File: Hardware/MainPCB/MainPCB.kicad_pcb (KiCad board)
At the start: 2 copper layers, 44 parts, among them J1 USB_B_Micro, J2 Conn_01x09_Female, J3 UART, Q1 NTR2101P, Q2 FDS9926A, U1 BQ24075, U2 BQ29700, U3 TLV75533PDBV, U4 ESP32-WROOM-32D, U5 TPS22919

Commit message: Eerste plaatsing van componenten op PCB
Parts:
- added C12: 10u/16V, Capacitor_SMD:CP_Elec_4x5.4, F.Cu at (55.8, 123.1)
- added C16: 3.3u/16V, Capacitor_SMD:CP_Elec_4x5.4, F.Cu at (55.8, 128.9)
- added C17: 3.3u/16V, Capacitor_SMD:CP_Elec_4x5.4, F.Cu at (63.6, 123.1)
- added C18: 10u/16V, Capacitor_SMD:CP_Elec_4x5.4, F.Cu at (63.6, 128.9)
- added C19: 10u/16V, Capacitor_SMD:CP_Elec_4x5.4, F.Cu at (71.3, 123.1)
- added R13: 680, Resistor_SMD:R_1206_3216Metric_Pad1.42x1.75mm_HandSolder, F.Cu at (54.9, 133.5)
- added R14: 680, Resistor_SMD:R_1206_3216Metric_Pad1.42x1.75mm_HandSolder, F.Cu at (60.9, 133.5)
- added U6: TPS22919, Package_TO_SOT_SMD:SOT-363_SC-70-6, F.Cu at (73.1, 113.9)
- added U7: TPS22919, Package_TO_SOT_SMD:SOT-363_SC-70-6, F.Cu at (80.9, 108.1)
- C10: value 47u -> 47u/10V
- C11, C13: value 100nF -> 0.1u
- C14: value 1u -> 3.3u/16V; footprint Capacitor_SMD:C_1206_3216Metric_Pad1.42x1.75mm_HandSolder -> Capacitor_SMD:CP_Elec_4x5.4
- C15: value 10u -> 10u/16V; footprint Capacitor_SMD:C_1206_3216Metric_Pad1.42x1.75mm_HandSolder -> Capacitor_SMD:CP_Elec_4x5.4
- C2: value 47u -> 47u/16V; footprint Capacitor_SMD:CP_Elec_5x5.9 -> Capacitor_SMD:CP_Elec_5x5.4
- C7: value 47u -> 47u/16V; footprint Capacitor_SMD:CP_Elec_4x5.4 -> Capacitor_SMD:CP_Elec_5x5.4
- JP1: value Jumper -> Stroommeetdraad
- moved C15 82.0 mm to (77.4, 129.3), turned to 180 degrees
- moved R11 81.4 mm to (81.1, 136.6), turned to 180 degrees
- moved U5 80.6 mm to (79.8, 115.0), turned to 180 degrees
- moved R12 79.7 mm to (81.1, 133.3), turned to 180 degrees
- moved J3 70.9 mm to (86.4, 135.9), turned to 180 degrees
- moved C11 70.2 mm to (84.9, 126.7), turned to 180 degrees
- moved U3 66.9 mm to (104.4, 99.4), turned to 270 degrees
- moved C2 65.7 mm to (136.7, 86.7), turned to 90 degrees
- moved D1 64.5 mm to (147.0, 103.4), turned to 90 degrees
- moved D2 60.3 mm to (147.0, 97.3), turned to 90 degrees
- moved C13 58.4 mm to (90.8, 126.9), turned to 180 degrees
- moved C12 58.2 mm to (90.8, 123.6), turned to 180 degrees
- moved EN1 55.1 mm to (94.2, 134.4), turned to 180 degrees
- moved R1 55.1 mm to (135.1, 95.7), turned to 90 degrees
- moved R2 52.4 mm to (126.7, 91.8), turned to 90 degrees
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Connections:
- C13 pad 1: +3V3 -> GND
- C13 pad 2: GND -> +3V3
- U4 pad 23: Net-(U4-Pad23) -> PowerS1
- U4 pad 27: Net-(U4-Pad27) -> PowerS2
- U4 pad 28: Net-(U4-Pad28) -> PowerS3
- U5 pad 3: Net-(U5-Pad3) -> PowerS1
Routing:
- net VSS: track 0.00 -> 66.7 mm
- net Net-(BT1-Pad2): track 0.00 -> 33.8 mm
- net +BATT: track 0.00 -> 30.7 mm
- net VDD1: track 0.00 -> 19.6 mm
- net Net-(Q2-Pad4): track 0.00 -> 19.2 mm
- net Vin: track 0.00 -> 18.4 mm
- net VDD2: track 0.00 -> 7.54 mm
- net Net-(Q2-Pad2): track 0.00 -> 6.79 mm
- net Net-(C8-Pad1): track 0.00 -> 6.63 mm
- net GND: track 0.00 -> 6.46 mm
- net Net-(Q2-Pad5): track 0.00 -> 3.81 mm
- net +3V3: track 0.00 -> 2.90 mm
- net Net-(R8-Pad1): track 0.00 -> 2.67 mm
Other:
- board outline added: 99.1 x 103.9 mm
- rule trace_min: 0.2 -> 0

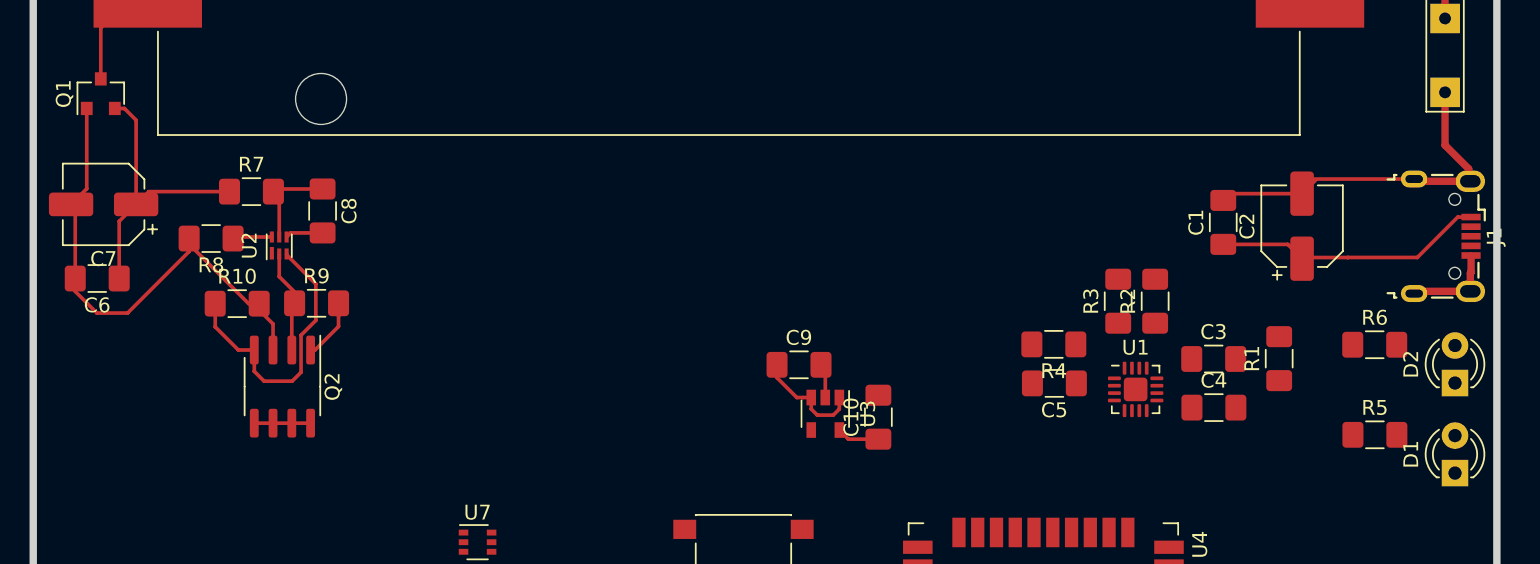
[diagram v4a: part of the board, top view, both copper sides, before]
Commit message: Aux pin verwijderd + aanpassing gedaan VSS naar -VBAT en GND op de juiste plaats gezet
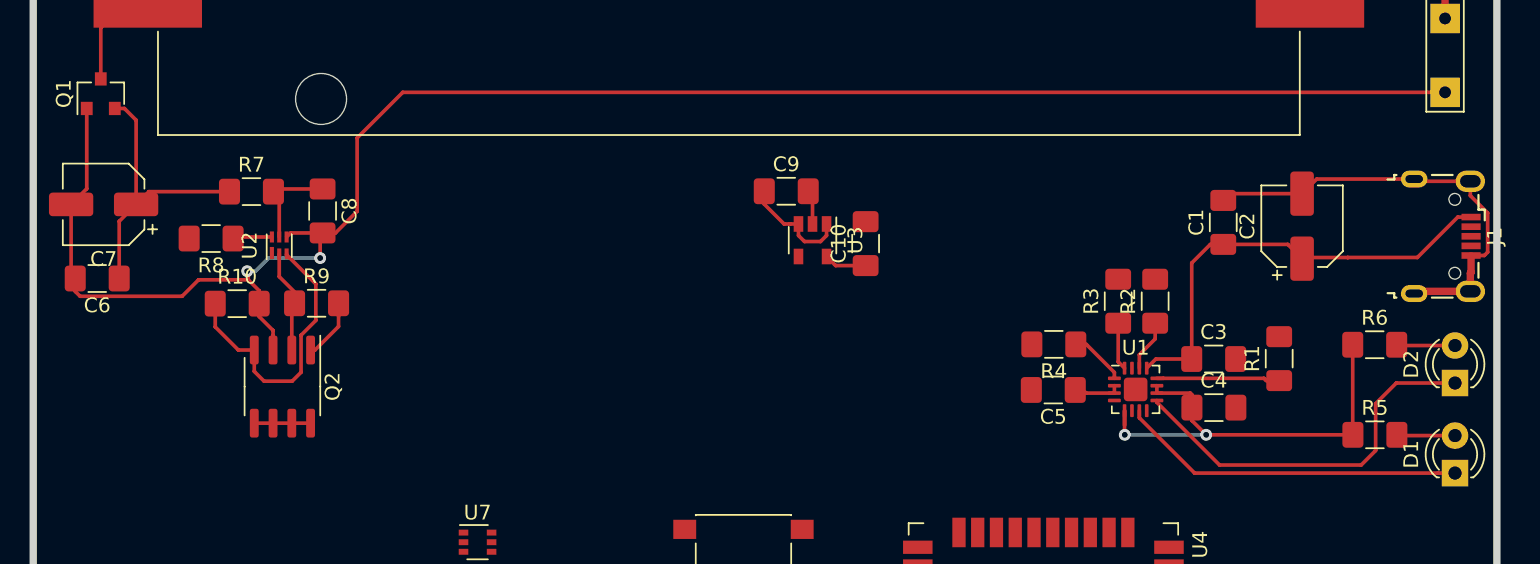
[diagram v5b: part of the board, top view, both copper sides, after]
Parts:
- moved C9 11.8 mm to (101.8, 84.3)
- moved U3 11.8 mm to (103.5, 87.6)
- moved C10 11.8 mm to (107.1, 87.9)
- moved C5 0.45 mm to (119.8, 97.8)
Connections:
- C1 pad 2: VSS -> GND
- C2 pad 2: VSS -> GND
- C3 pad 2: VSS -> Net-(C3-Pad2)
- C4 pad 2: VSS -> GND
- C5 pad 2: VSS -> GND
- C6 pad 2: VSS -> -BATT
- C7 pad 2: VSS -> -BATT
- C8 pad 2: VSS -> -BATT
- J1 pad 5: VSS -> GND
- J1 pad 6: VSS -> GND
- JP1 pad 2: VSS -> -BATT
- Q1 pad 1: VSS -> -BATT
- Q2 pad 3: VSS -> -BATT
- R1 pad 2: VSS -> GND
- R10 pad 2: VSS -> -BATT
- R2 pad 2: VSS -> GND
- R3 pad 2: VSS -> GND
- R4 pad 2: VSS -> GND
- R8 pad 2: VSS -> GND
- U1 pad 15: VSS -> GND
- U1 pad 17: VSS -> GND
- U1 pad 4: VSS -> GND
- U1 pad 6: VSS -> GND
- U1 pad 8: VSS -> GND
- U2 pad 4: VSS -> -BATT
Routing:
- net -BATT: track 0.00 -> 123.8 mm, vias 0 -> 2
- net VSS: track 66.7 -> 0.00 mm
- net VDD2: track 7.54 -> 37.7 mm, vias 0 -> 2
- net GND: track 6.46 -> 36.6 mm
- net Net-(D2-Pad1): track 0.00 -> 26.2 mm
- net Net-(D1-Pad1): track 0.00 -> 23.4 mm
- net Vin: track 18.4 -> 30.9 mm
- net Net-(R1-Pad1): track 0.00 -> 8.34 mm
- net Net-(D2-Pad2): track 0.00 -> 3.97 mm
- net Net-(D1-Pad2): track 0.00 -> 3.96 mm
- net Net-(R4-Pad1): track 0.00 -> 3.80 mm
- net Net-(R2-Pad1): track 0.00 -> 3.49 mm
- net VDD1: track 19.6 -> 23.0 mm
- net Net-(R3-Pad1): track 0.00 -> 3.22 mm

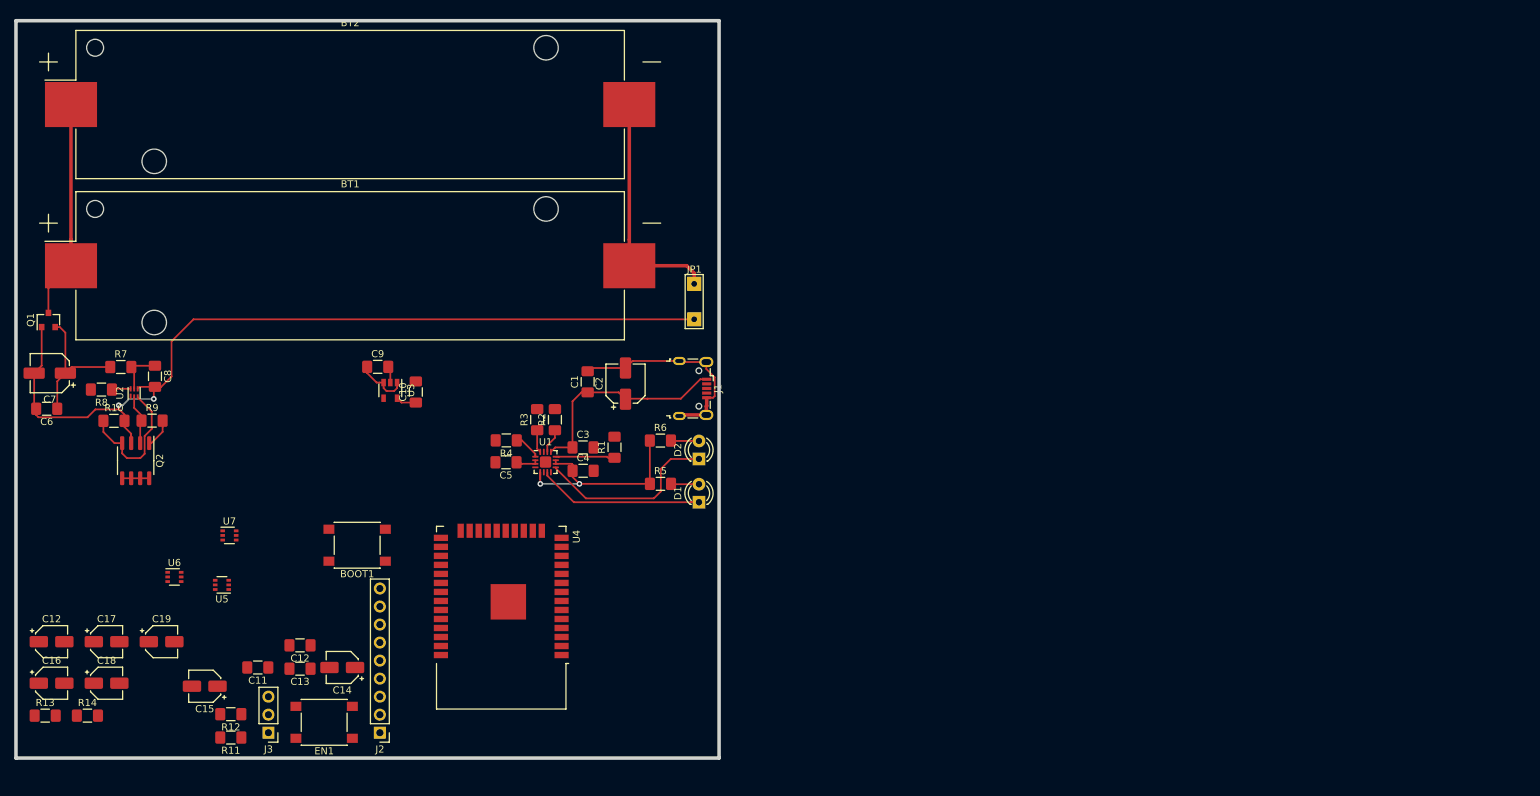
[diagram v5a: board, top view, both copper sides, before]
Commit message: routed mcu part of main pcb
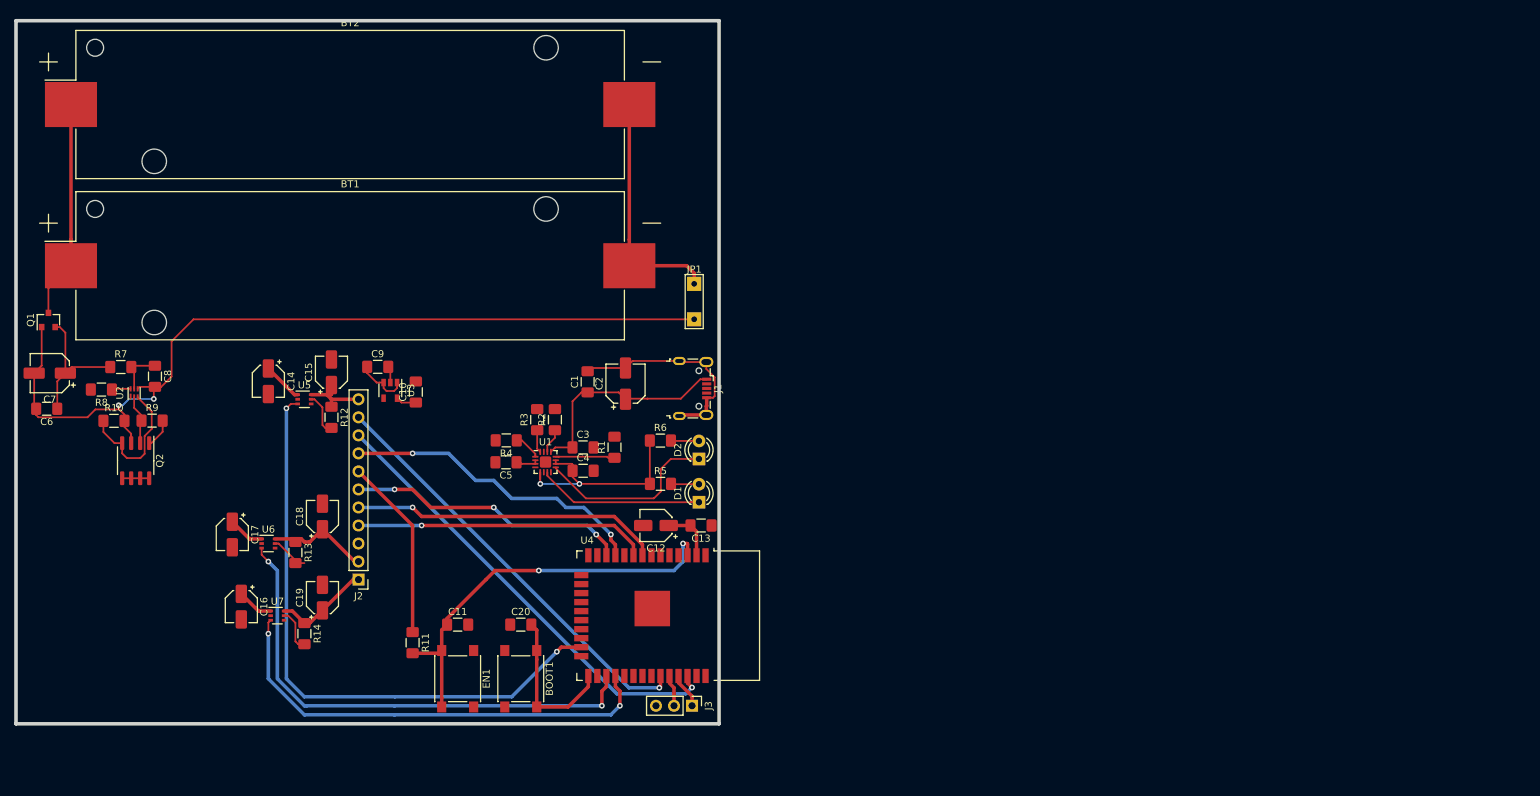
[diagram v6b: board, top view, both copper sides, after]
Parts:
- removed the C12 at (90.8, 123.6)
- added C20: 0.1u, Capacitor_SMD:C_1206_3216Metric_Pad1.42x1.75mm_HandSolder, F.Cu at (121.9, 120.7)
- J2: value Conn_01x09_Female -> Conn_01x11; footprint Connector_PinHeader_2.54mm:PinHeader_1x09_P2.54mm_Vertical -> Connector_PinHeader_2.54mm:PinHeader_1x11_P2.54mm_Vertical
- moved C12 86.7 mm to (141.0, 106.7), turned to 180 degrees
- moved C13 60.0 mm to (147.3, 106.7)
- moved J3 59.8 mm to (146.1, 132.1), turned to 270 degrees
- moved C15 47.7 mm to (95.2, 85.1), turned to 90 degrees
- moved R12 44.2 mm to (95.2, 91.4), turned to 270 degrees
- moved R13 42.1 mm to (90.2, 110.5), turned to 270 degrees
- moved C14 41.6 mm to (86.4, 86.4), turned to 270 degrees
- moved C18 38.4 mm to (94.0, 105.4), turned to 90 degrees
- moved R14 32.7 mm to (91.4, 121.9), turned to 270 degrees
- moved BOOT1 29.8 mm to (121.9, 128.3), turned to 270 degrees
- moved R11 28.9 mm to (106.7, 123.2), turned to 270 degrees
- moved C16 28.8 mm to (82.5, 118.1), turned to 270 degrees
- moved C11 28.8 mm to (113.0, 120.7), turned to 0 degrees
- moved U5 28.6 mm to (91.4, 88.9), turned to 0 degrees
- moved C19 23.5 mm to (94.0, 116.8), turned to 90 degrees
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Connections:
- C15 pad 1: Net-(C15-Pad1) -> CCS811_3V3
- C18 pad 1: Net-(C18-Pad1) -> AUDIO_3V3
- C19 pad 1: Net-(C19-Pad1) -> AMG8833_3V3
- J2 pad 1: Detector_out -> AMG8833_3V3
- J2 pad 2: AUX -> AUDIO_3V3
- J2 pad 3: nWake -> GND
- J2 pad 4: Int_CCSB11 -> Detector_out
- J2 pad 5: Int_AMG8833 -> nWake
- J2 pad 6: GND -> Int_CCSB11
- J2 pad 7: SCL -> +3V3
- J2 pad 8: SDA -> Int_AMG8833
- J2 pad 9: +3V3 -> SCL
- R12 pad 1: Net-(C15-Pad1) -> CCS811_3V3
- R13 pad 1: Net-(C18-Pad1) -> AUDIO_3V3
- R14 pad 1: Net-(C19-Pad1) -> AMG8833_3V3
- U4 pad 6: AUX -> Net-(U4-Pad6)
- U5 pad 6: Net-(C15-Pad1) -> CCS811_3V3
- U6 pad 6: Net-(C18-Pad1) -> AUDIO_3V3
- U7 pad 6: Net-(C19-Pad1) -> AMG8833_3V3
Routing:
- net PowerS1: track 0.00 -> 85.4 mm, vias 0 -> 2
- net PowerS2: track 0.00 -> 71.1 mm, vias 0 -> 2
- net PowerS3: track 0.00 -> 65.0 mm, vias 0 -> 2
- net SCL: track 0.00 -> 64.3 mm, vias 0 -> 1
- net SDA: track 0.00 -> 59.9 mm, vias 0 -> 1
- net Net-(C11-Pad1): track 0.00 -> 58.4 mm, vias 0 -> 2
- net +3V3: track 2.90 -> 52.2 mm
- net nWake: track 0.00 -> 43.7 mm, vias 0 -> 1
- net Int_AMG8833: track 0.00 -> 43.5 mm, vias 0 -> 2
- net Detector_out: track 0.00 -> 41.4 mm, vias 0 -> 1
- net Int_CCSB11: track 0.00 -> 39.6 mm, vias 0 -> 3
- net Net-(BOOT1-Pad1): track 0.00 -> 21.9 mm
- net AUDIO_3V3: track 0.00 -> 14.6 mm
- net AMG8833_3V3: track 0.00 -> 13.7 mm
- net CCS811_3V3: track 0.00 -> 9.97 mm
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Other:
- board size 99.1 x 103.9 mm -> 99.1 x 99.1 mm

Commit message: Finished MainPCB + generated gerber files + aanpassingen BOM
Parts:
- added REF**: MountingHole_3.2mm_M3, MountingHole:MountingHole_3.2mm_M3, F.Cu at (58.5, 130.1)
- added REF**: MountingHole_3.2mm_M3, MountingHole:MountingHole_3.2mm_M3, F.Cu at (140.8, 39.9)
- moved R9 8.12 mm to (73.9, 99.0)
- moved C8 8.12 mm to (74.3, 92.8)
- moved C6 8.12 mm to (59.1, 97.3)
- moved R8 8.12 mm to (66.8, 94.6)
- moved C7 8.12 mm to (59.5, 92.3)
- moved Q1 8.12 mm to (59.3, 84.8)
- moved Q2 8.12 mm to (71.6, 104.6)
- moved R10 8.12 mm to (68.5, 99.0)
- moved R7 8.12 mm to (69.5, 91.5)
- moved U2 8.12 mm to (71.4, 95.1)
- moved C12 6.43 mm to (134.6, 106.3)
- moved J3 6.24 mm to (139.8, 132.7)
- moved C13 6.15 mm to (141.2, 107.1)
- moved R11 5.79 mm to (100.9, 123.5)
- moved C2 5.61 mm to (131.1, 86.1)
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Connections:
- C3 pad 2: Net-(C3-Pad2) -> GND
- J2 pad 10: SDA -> SCL
- J2 pad 4: Detector_out -> Int_CCSB11
- J2 pad 5: nWake -> Detector_out
- J2 pad 6: Int_CCSB11 -> nWake
- J2 pad 9: SCL -> SDA
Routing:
- net +3V3: track 52.2 -> 195.9 mm
- net VDD1: track 23.0 -> 84.1 mm, vias 0 -> 2
- net VDD2: track 37.7 -> 71.2 mm, vias 2 -> 5
- net PowerS1: track 85.4 -> 67.2 mm
- net +BATT: track 30.7 -> 44.7 mm
- net SCL: track 64.3 -> 73.9 mm
- net SDA: track 59.9 -> 69.4 mm
- net Int_CCSB11: track 39.6 -> 32.4 mm, vias 3 -> 0
- net PowerS2: track 71.1 -> 64.7 mm
- net GND: track 36.6 -> 42.7 mm, vias 0 -> 11
- net PowerS3: track 65.0 -> 59.5 mm
- net nWake: track 43.7 -> 39.3 mm, vias 1 -> 0
- net Detector_out: track 41.4 -> 37.1 mm, vias 1 -> 0
- net Net-(BT1-Pad2): track 33.8 -> 31.2 mm
- net -BATT: track 123.8 -> 121.9 mm
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- added copper zone on B.Cu, net GND
- added copper zone on F.Cu, net GND
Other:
- board size 99.1 x 99.1 mm -> 91.7 x 99.1 mm
- board text added: "3V3"
- board text added: "AMG8833_3V3"
- board text added: "AUDIO_3V3"
- board text added: "CCS811_3V3"
- board text added: "Detect_out"
- board text added: "GND"
- board text added: "INT_AMG8833"
- board text added: "Int_CCSB11"
- board text added: "MainPCB Cosy cafetaria Ref-1"
- board text added: "SCL"
- board text added: "SDA"
- board text added: "nWake"
